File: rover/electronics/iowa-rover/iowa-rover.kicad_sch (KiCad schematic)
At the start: 10 parts, among them J3 Conn_01x02

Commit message: draw board
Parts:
- C1: value (none) -> C; footprint (none) -> Capacitor_THT:C_Disc_D4.3mm_W1.9mm_P5.00mm
- J1: value (none) -> Adafruit_USB_C; footprint (none) -> SMM:Adafruit_USB_C
- J2: value (none) -> Conn_01x02; footprint (none) -> SMM:TerminalBlock-2_P5.08mm_small
- J3: footprint (none) -> SMM:TerminalBlock-2_P5.08mm_small
- R1: value (none) -> 5.1k; footprint (none) -> SMM:Resistor_L6.3mm_D2.5mm_P10.16mm_Horizontal
- R2: footprint (none) -> SMM:Resistor_L6.3mm_D2.5mm_P10.16mm_Horizontal
- RV1: value (none) -> R_Potentiometer; footprint (none) -> SMM:Rover_Trimpot
- U1: value (none) -> Adafruit_Metro_Mini; footprint (none) -> SMM:Metro-Mini
- U2: value (none) -> Adafruit_RFM69HCW_Breakout; footprint (none) -> SMM:Adafruit RFM69HCW Breakout
- U3: value (none) -> Adafruit_TB6612_Breakout; footprint (none) -> SMM:Adafruit_TB6612_Breakout
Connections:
- net +5V: now also U3.1 (Vmotor), U3.2 (VCC); no longer U3. (Vmotor)
- net AIN1: now also U3.8 (AIN1); no longer U3. (Vmotor)
- net AIN2: now also U3.9 (AIN2); no longer U3. (Vmotor)
- net BIN1: now also U3.6 (BIN1); no longer U3. (Vmotor)
- net BIN2: now also U3.5 (BIN2); no longer U3. (Vmotor)
- net GND: now also J1.S1 (SHIELD), U3.13 (GND), U3.14 (GND), U3.3 (GND); no longer U3. (Vmotor)
- net PWMA: now also U3.10 (PWMA); no longer U3. (Vmotor)
- net PWMB: now also U3.4 (PWMB); no longer U3. (Vmotor)
- net MB1: now reaches J3.1 (Pin_1)
- net MB1: now also U3.15 (MOT_B1); no longer U3. (Vmotor)
- net MB2: now reaches J3.2 (Pin_2)
- net MB2: now also U3.16 (MOT_B2); no longer U3. (Vmotor)
- net MA1: now reaches J2.1 (Pin_1)
- net MA1: now also U3.11 (MOT_A1); no longer U3. (Vmotor)
- net MA2: now reaches J2.2 (Pin_2)
- net MA2: now also U3.12 (MOT_A2); no longer U3. (Vmotor)
- no-connect marks 19 -> 18
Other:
- moved on the sheet: J2, J3

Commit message: update
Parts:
- added SW1: SW_SPDT, SMM:SW_EG1218, symbol Switch:SW_SPDT
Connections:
- net +5V: now also SW1.1 (A)
- net GND: now also SW1.3 (C)
- net at U1.10 (A1): now also SW1.2 (B)
- no-connect marks 18 -> 17
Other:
- moved on the sheet: C1, U2

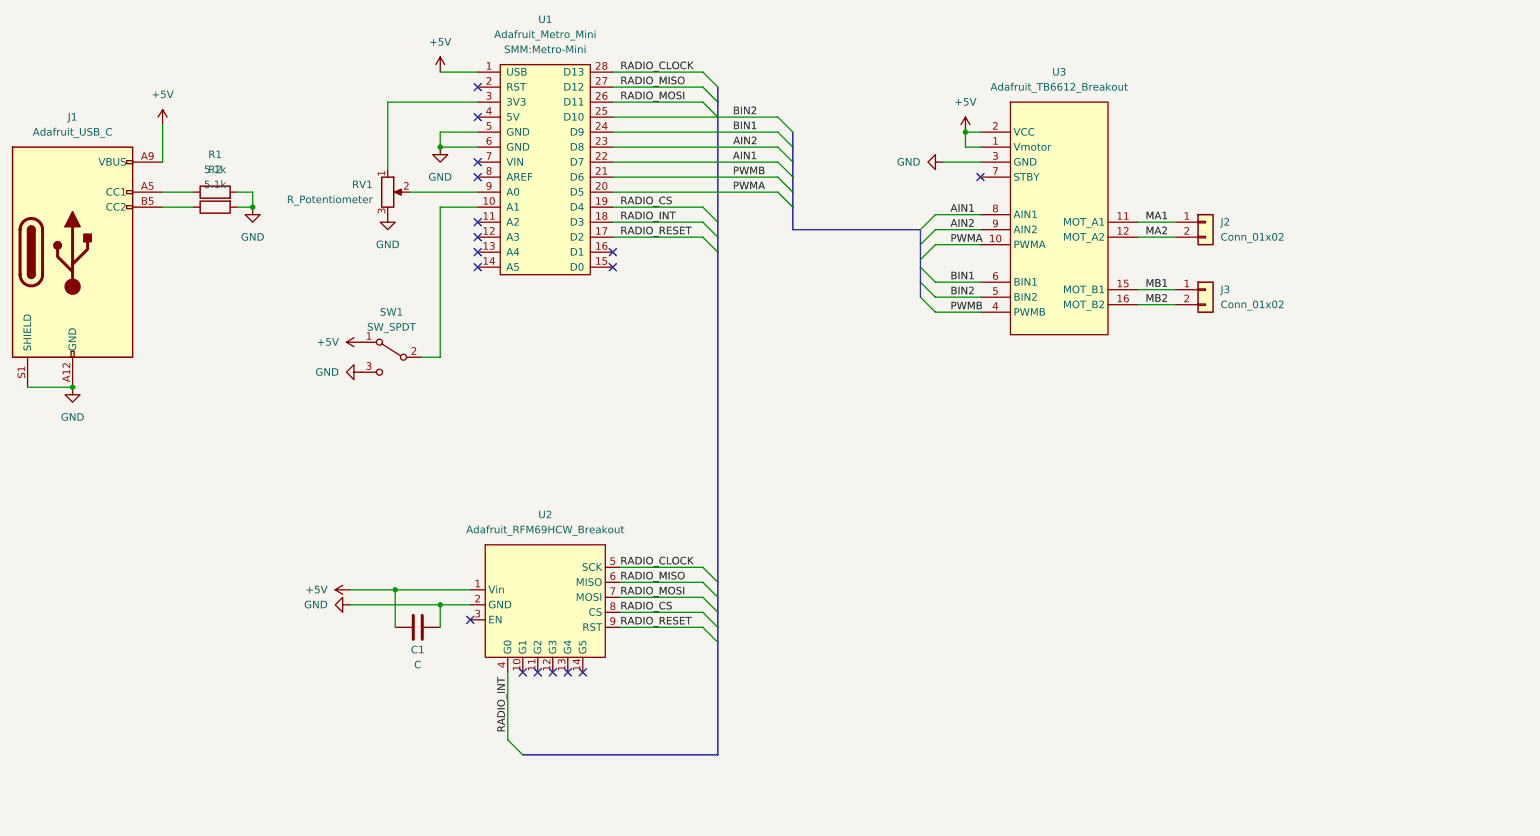
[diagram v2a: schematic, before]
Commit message: update radio power and add electronics PDF and readme
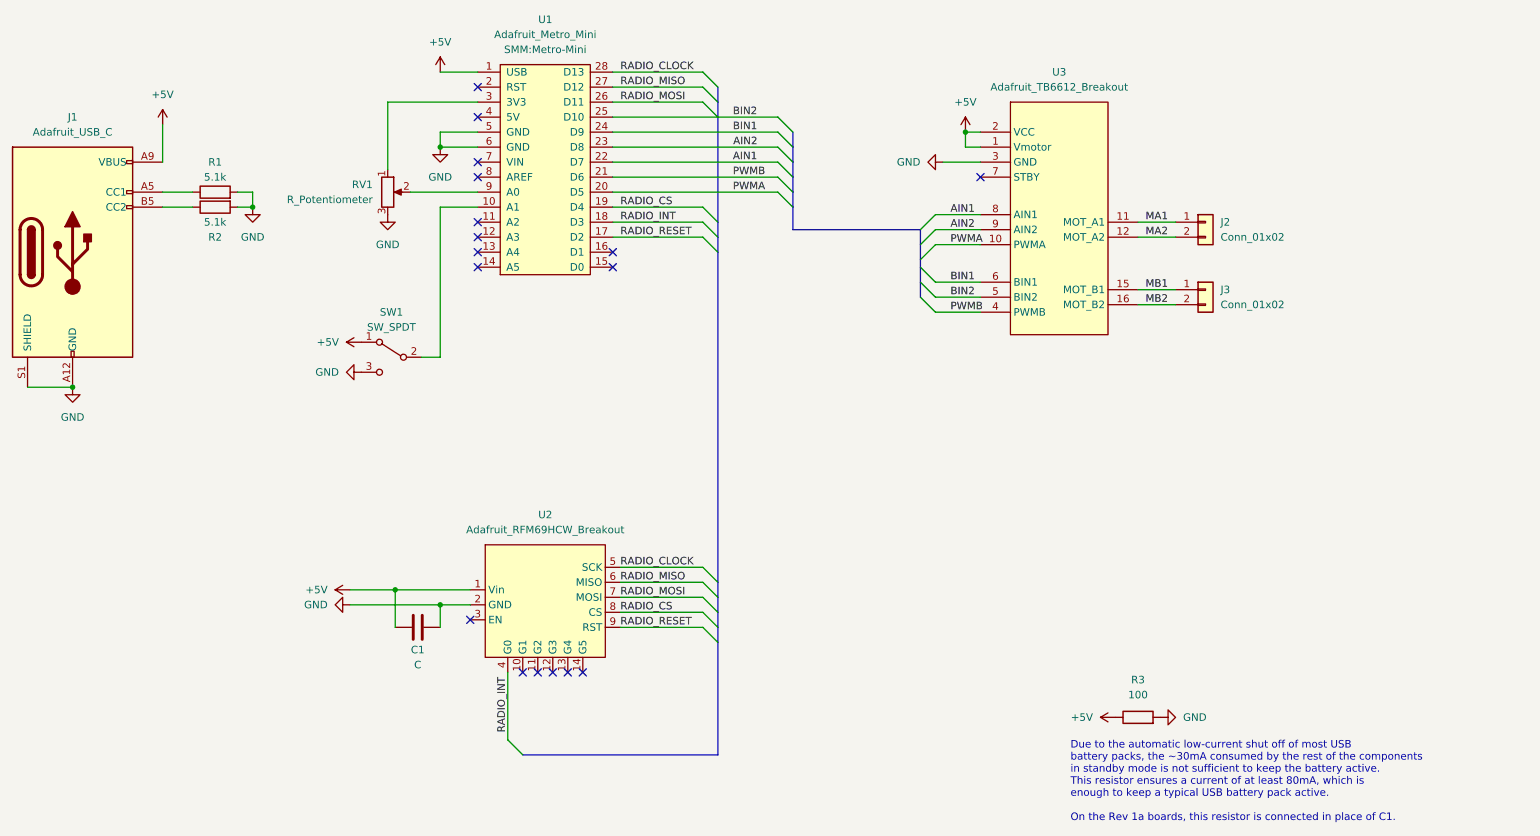
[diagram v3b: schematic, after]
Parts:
- added R3: 100, symbol Device:R
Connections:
- net +5V: now also R3.1
- net GND: now also R3.2
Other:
- note added: "Due to the automatic low-current shut off of most USB battery packs, the ~30mA consumed by the rest of the components in standby mode is not sufficient to keep the battery active. This resistor ensures a current of at least 80mA, which is enough to keep a typical USB battery pack active. On the Rev 1a boards, this resistor is connected in place of C1."
- company: (none) -> Science Museum of Minnesota
- title: (none) -> Iowa Science Rover - Rover Controller
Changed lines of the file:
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@@
 (kicad_sch (version 20230121) (generator eeschema)
   (paper "A4")
+  (title_block
+    (title "Iowa Science Rover - Rover Controller")
+    (date "2023-10-04")
+    (rev "2")
+    (company "Science Museum of Minnesota")
+    (comment 1 "Kate Swanson")
+  )
   (junction (at 40.64 81.28) (diameter 0) (color 0 0 0 0)
   )
@@
     (stroke (width 0) (type default))
   )
+  (text "Due to the automatic low-current shut off of most USB\nbattery packs, the ~30mA consumed by the rest of the components\nin standby mode is not sufficient to keep the battery active.\nThis resistor ensures a current of at least 80mA, which is\nenough to keep a typical USB battery pack active.\n\nOn the Rev 1a boards, this resistor is connected in place of C1."
+    (at 209.55 154.94 0)
+    (effects (font (size 1.27 1.27)) (justify left bottom))
+  )
   (label "PWMB" (at 189.23 68.58 0) (fields_autoplaced)
     (effects (font (size 1.27 1.27)) (justify left bottom))
@@
   )
   (symbol (lib_id "Device:R") (at 64.77 48.26 90) (unit 1)
-    (in_bom yes) (on_board yes) (dnp no) (fields_autoplaced)
-    (property "Reference" "R1" (at 64.77 41.91 90)
-      (effects (font (size 1.27 1.27)))
-    )
-    (property "Value" "5.1k" (at 64.77 44.45 90)
+    (in_bom yes) (on_board yes) (dnp no)
+    (property "Reference" "R1" (at 64.77 43.18 90)
+      (effects (font (size 1.27 1.27)))
+    )
+    (property "Value" "5.1k" (at 64.77 45.72 90)
       (effects (font (size 1.27 1.27)))
     )
@@
   )
   (symbol (lib_id "Device:R") (at 64.77 50.8 90) (mirror x) (unit 1)
-    (in_bom yes) (on_board yes) (dnp no) (fields_autoplaced)
-    (property "Reference" "R2" (at 64.77 44.45 90)
-      (effects (font (size 1.27 1.27)))
-    )
-    (property "Value" "5.1k" (at 64.77 46.99 90)
+    (in_bom yes) (on_board yes) (dnp no)
+    (property "Reference" "R2" (at 64.77 55.88 90)
+      (effects (font (size 1.27 1.27)))
+    )
+    (property "Value" "5.1k" (at 64.77 53.34 90)
       (effects (font (size 1.27 1.27)))
     )
@@
         (path "/41c9c3b8-2883-4fdc-b499-17634b4fcf10"
           (reference "#PWR011") (unit 1)
+        )
+      )
+    )
+  )
+  (symbol (lib_name "GND_1") (lib_id "power:GND") (at 224.79 137.16 90) (unit 1)
+    (in_bom yes) (on_board yes) (dnp no) (fields_autoplaced)
+    (property "Reference" "#PWR014" (at 231.14 137.16 0)
+      (effects (font (size 1.27 1.27)) hide)
+    )
+    (property "Value" "GND" (at 228.6 137.16 90)
+      (effects (font (size 1.27 1.27)) (justify right))
+    )
+    (property "Footprint" "" (at 224.79 137.16 0)
+      (effects (font (size 1.27 1.27)) hide)
+    )
+    (property "Datasheet" "" (at 224.79 137.16 0)
+      (effects (font (size 1.27 1.27)) hide)
+    )
+    (pin "1")
+    (instances
+      (project "iowa-rover"
+        (path "/41c9c3b8-2883-4fdc-b499-17634b4fcf10"
+          (reference "#PWR014") (unit 1)
         )
       )
@@
     )
   )
+  (symbol (lib_name "+5V_1") (lib_id "power:+5V") (at 217.17 137.16 90) (unit 1)
+    (in_bom yes) (on_board yes) (dnp no) (fields_autoplaced)
+    (property "Reference" "#PWR013" (at 220.98 137.16 0)
+      (effects (font (size 1.27 1.27)) hide)
+    )
+    (property "Value" "+5V" (at 213.36 137.16 90)
+      (effects (font (size 1.27 1.27)) (justify left))
+    )
+    (property "Footprint" "" (at 217.17 137.16 0)
+      (effects (font (size 1.27 1.27)) hide)
+    )
+    (property "Datasheet" "" (at 217.17 137.16 0)
+      (effects (font (size 1.27 1.27)) hide)
+    )
+    (pin "1")
+    (instances
+      (project "iowa-rover"
+        (path "/41c9c3b8-2883-4fdc-b499-17634b4fcf10"
+          (reference "#PWR013") (unit 1)
+        )
+      )
+    )
+  )
   (symbol (lib_id "Connector_Generic:Conn_01x02") (at 232.41 53.34 0) (unit 1)
     (in_bom yes) (on_board yes) (dnp no) (fields_autoplaced)
@@
         )
       )
+    )
+  )
+  (symbol (lib_id "Device:R") (at 220.98 137.16 90) (unit 1)
+    (in_bom yes) (on_board yes) (dnp no) (fields_autoplaced)
+    (property "Reference" "R3" (at 220.98 130.81 90)
+      (effects (font (size 1.27 1.27)))
+    )
+    (property "Value" "100" (at 220.98 133.35 90)
+      (effects (font (size 1.27 1.27)))
+    )
+    (property "Footprint" "" (at 220.98 138.938 90)
+      (effects (font (size 1.27 1.27)) hide)
+    )
+    (property "Datasheet" "~" (at 220.98 137.16 0)
+      (effects (font (size 1.27 1.27)) hide)
+    )
+    (pin "1")
+    (pin "2")
+    (instances
+      (project "iowa-rover"
+        (path "/41c9c3b8-2883-4fdc-b499-17634b4fcf10"
+          (reference "R3") (unit 1)
+        )
+      )
